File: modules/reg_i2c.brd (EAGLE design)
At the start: 31.7 x 12.7 mm, 11 parts, among them J3 MOLEX_MINILITE_TRAP_2, J4 MOLEX_MINILITE_TRAP_2, U1 P82B715D

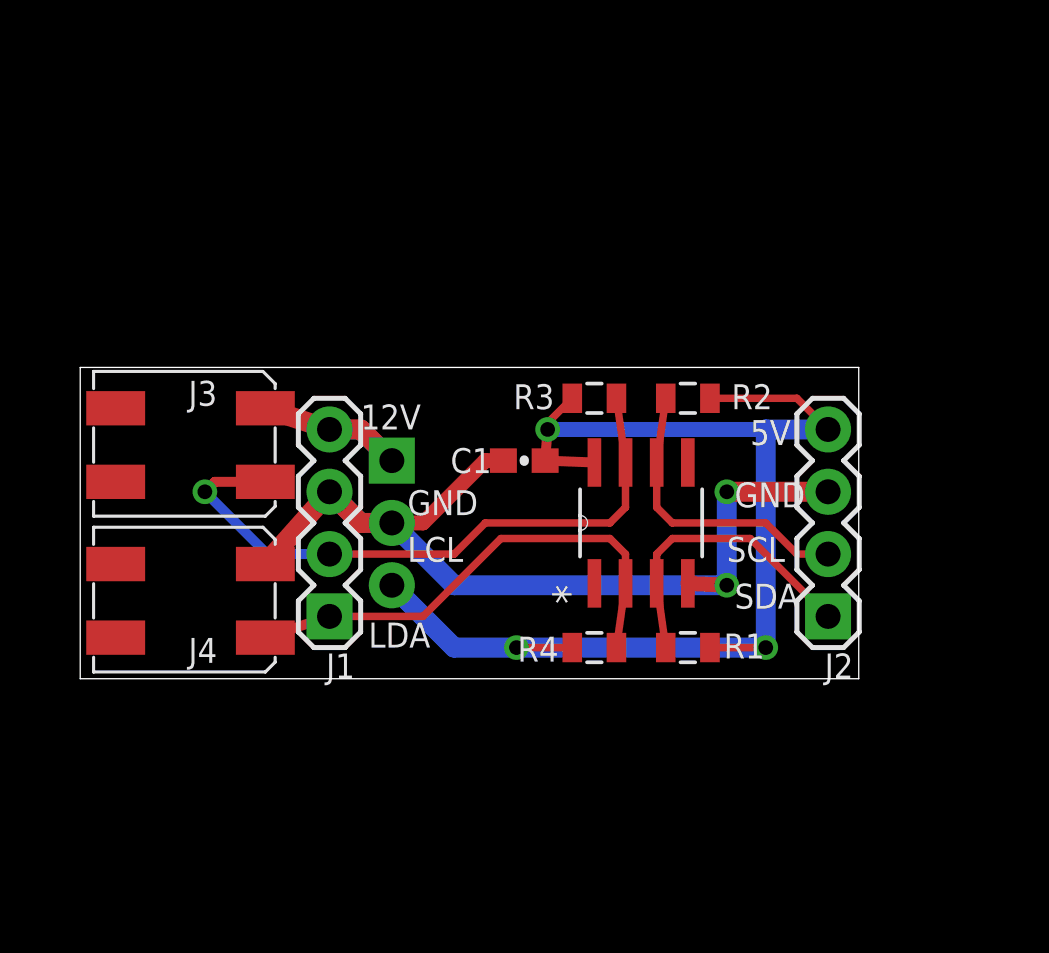
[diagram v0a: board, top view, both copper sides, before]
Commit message: Change reg_i2c to use a 2x8 header
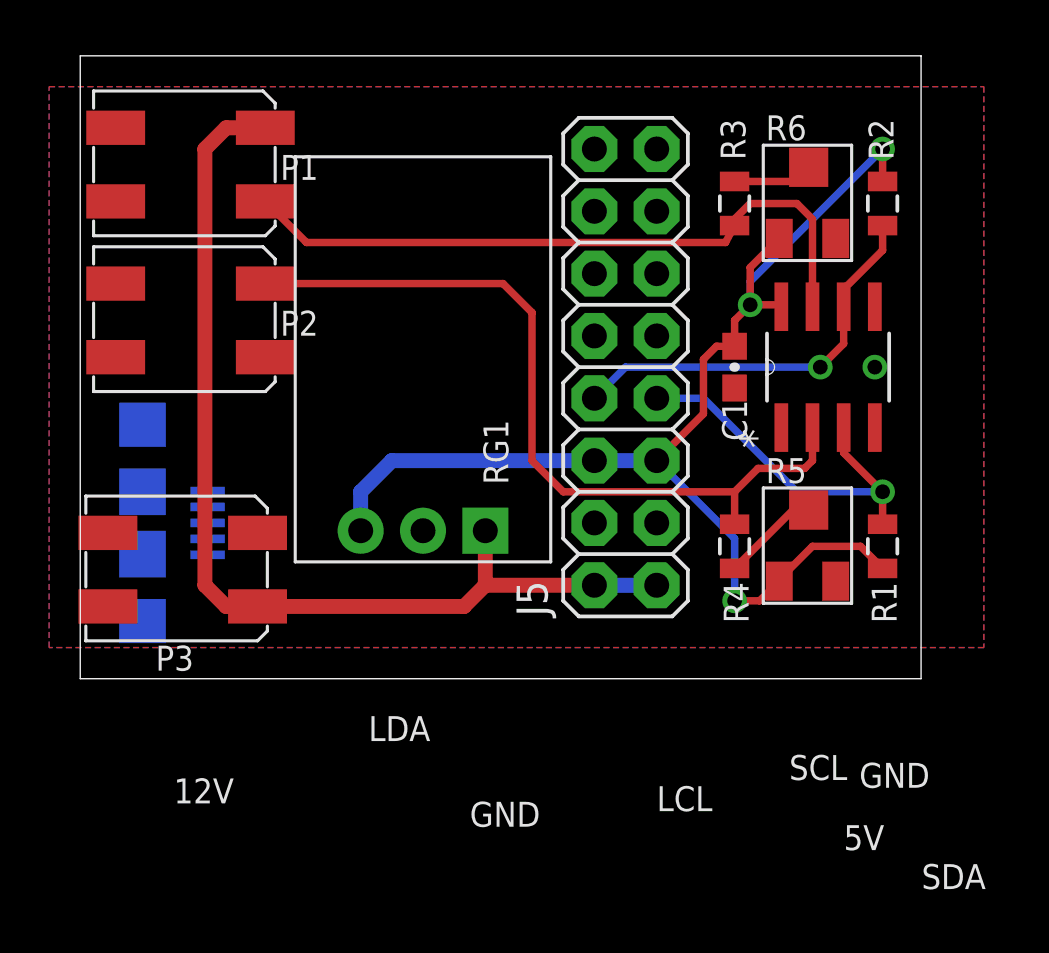
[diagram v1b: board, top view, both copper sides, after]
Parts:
- removed J1: (no value), SparkFun-Connectors:1X04
- removed J3, J4: MOLEX_MINILITE_TRAP_2, Puffin:MOLEX_MINILITE_TRAP_2
- added J5: (no value), SparkFun-Connectors:2X8
- added P1, P2, P3: MOLEX_MINILITE_TRAP_2, Puffin:MOLEX_MINILITE_TRAP_2
- added R5, R6: (no value), Puffin:POT_3MM
- J2: value (none) -> USB-MICROB; device SparkFun-Connectors:1X04 -> SparkFun-Connectors:USB-MICROB
- moved J2 28.2 mm to (2.54, 6.35), flipped to the bottom
- moved R2 11.2 mm to (32.7, 19.4), turned to 90 degrees
- moved U1 9.92 mm to (30.5, 12.7)
- moved R3 9.78 mm to (26.7, 19.4), turned to 90 degrees
- moved C1 9.38 mm to (26.7, 12.7), turned to 270 degrees
- moved R1 8.95 mm to (32.7, 5.40), turned to 270 degrees
- moved R4 7.05 mm to (26.7, 5.40), turned to 270 degrees
- moved RG1 1.31 mm to (14.0, 6.03), flipped to the top, turned to 0 degrees
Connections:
- removed net 12V: J1.4, J3.2, RG1.1
- removed net 5V: C1.1, J2.4, R1.2, R2.2, R3.2, R4.2, RG1.3, U1.8
- removed net N$1: J2.1, R1.1, U1.3
- removed net N$2: J2.2, R2.1, U1.6
- new net 3.3V: C1.1, J5.5, J5.6, R1.2, R2.2, R5.3, R6.3, RG1.3, U1.8
- new net IO1: J5.9
- new net IO2: J5.10
- new net IO3: J5.11
- new net IO4: J5.12
- new net IO5: J5.13
- new net IO6: J5.14
- new net IO7: J5.15
- new net IO8: J5.16
- new net N$3: R3.2, R6.2
- new net N$4: R4.2, R5.2
- new net SCL: J5.7, R1.1, U1.3
- new net SDA: J5.8, R2.1, U1.6
- new net VIN: J2.VBUS, J5.1, J5.2, P1.2, P3.1, RG1.1
- net GND: now also J2.GND, J2.MT1, J2.MT2, J5.3, J5.4, P2.1, P3.2; no longer J1.3, J2.3, J4.2
- net N$6: now also P1.1; no longer J1.2, J3.1
- net N$7: now also P2.2; no longer J1.1, J4.1
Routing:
- net 5V: track 51.5 -> 0.00 mm, vias 3 -> 0
- net 3.3V: track 0.00 -> 51.3 mm, vias 0 -> 3
- net VIN: track 0.00 -> 42.0 mm
- net GND: track 39.9 -> 0.00 mm, vias 2 -> 1
- net SDA: track 0.00 -> 16.6 mm, vias 0 -> 1
- net SCL: track 0.00 -> 15.4 mm, vias 0 -> 1
- net N$1: track 12.4 -> 0.00 mm
- net N$7: track 20.2 -> 32.5 mm
- net N$2: track 12.2 -> 0.00 mm
- net 12V: track 8.89 -> 0.00 mm
- net N$4: track 0.00 -> 4.00 mm
- net N$3: track 0.00 -> 3.26 mm
- net N$6: track 26.1 -> 27.8 mm, vias 1 -> 0
- added copper zone on layer 1, net GND
- added copper zone on layer 16, net GND
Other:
- board size 31.7 x 12.7 mm -> 34.3 x 25.4 mm

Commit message: Gate 4, and misc updates
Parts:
- removed J2: USB-MICROB, SparkFun-Connectors:USB-MICROB
- added U$1: USB_MICRO, Puffin:USB_MICROB_MOLEX
- moved J5 18.9 mm to (29.8, 21.6), turned to 270 degrees
- moved R4 15.5 mm to (20.6, 19.7), turned to 90 degrees
- moved R3 14.9 mm to (20.6, 5.71), turned to 270 degrees
- moved P1 6.35 mm to (4.45, 14.6)
- moved P2 6.35 mm to (4.45, 21.0)
- moved C1 6.04 mm to (20.6, 13.0)
- moved R5 6.04 mm to (21.9, 3.49)
- moved R6 6.04 mm to (21.9, 17.5)
- moved R1 6.04 mm to (26.7, 5.71)
- moved R2 6.04 mm to (26.7, 19.7)
- moved U1 6.04 mm to (24.4, 13.0)
- moved P3 0.32 mm to (4.45, 4.45)
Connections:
- net IO2 renamed IO15
- net IO3 renamed IO17
- net IO5 renamed IO27
- net IO7 renamed IO22
- net IO8 renamed IO23
- removed net IO1: J5.9
- removed net IO6: J5.14
- new net IO14: J5.8
- new net IO18: J5.12
- net 3.3V: now also J5.1; no longer J5.5, J5.6
- net GND: now also J5.14, J5.6, J5.9, U$1.5; no longer J2.GND, J2.MT1, J2.MT2, J5.3, J5.4
- net IO4: now also J5.7; no longer J5.12
- net N$3: now also R4.2; no longer R3.2
- net N$4: now also R3.2; no longer R4.2
- net N$6: now also P2.2, R4.1; no longer P1.1, R3.1
- net N$7: now also P1.1, R3.1; no longer P2.2, R4.1
- net SCL: now also J5.5; no longer J5.7
- net SDA: now also J5.3; no longer J5.8
- net VIN: now also J5.4, U$1.1; no longer J2.VBUS, J5.1
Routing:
- net VIN: track 42.0 -> 74.7 mm, vias 0 -> 1
- net GND: track 0.00 -> 29.3 mm
- net 3.3V: track 51.3 -> 68.4 mm, vias 3 -> 1
- net N$7: track 32.5 -> 22.9 mm
- net SDA: track 16.6 -> 8.30 mm, vias 1 -> 0
- net N$6: track 27.8 -> 22.9 mm
- net SCL: track 15.4 -> 12.5 mm, vias 1 -> 0
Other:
- board text added: "3V3"
- board text added: "3v3"
- board text added: "VIN"
- board text removed: "12V"
